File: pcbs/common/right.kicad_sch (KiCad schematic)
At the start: 89 parts, among them J2 TRS

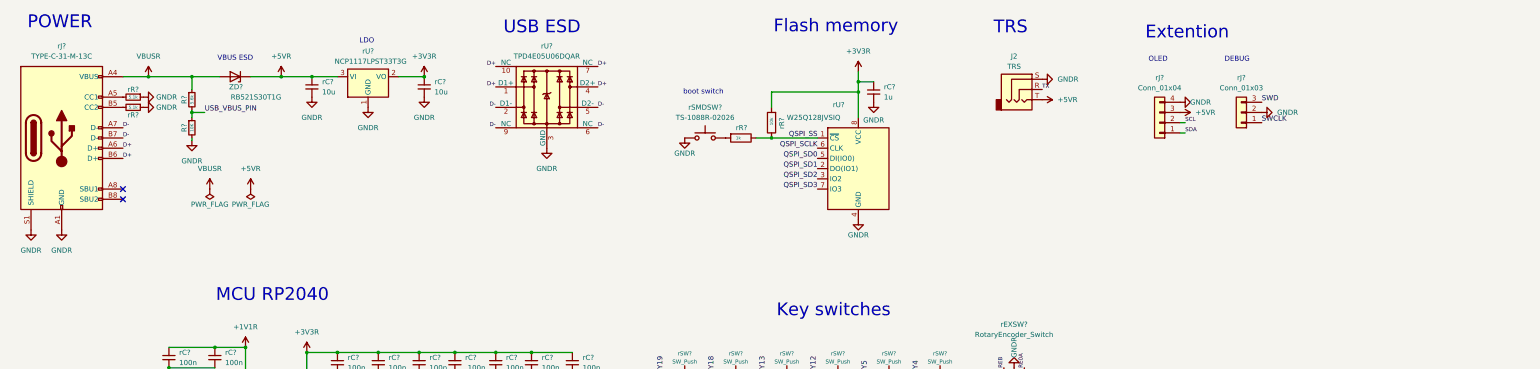
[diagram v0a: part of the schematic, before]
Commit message: Split comms through USB-C. Added more ESD.
Made a switch from TRS to USB-C for better ESD and short-circuit prevention. Added ferrite beads on external connections.
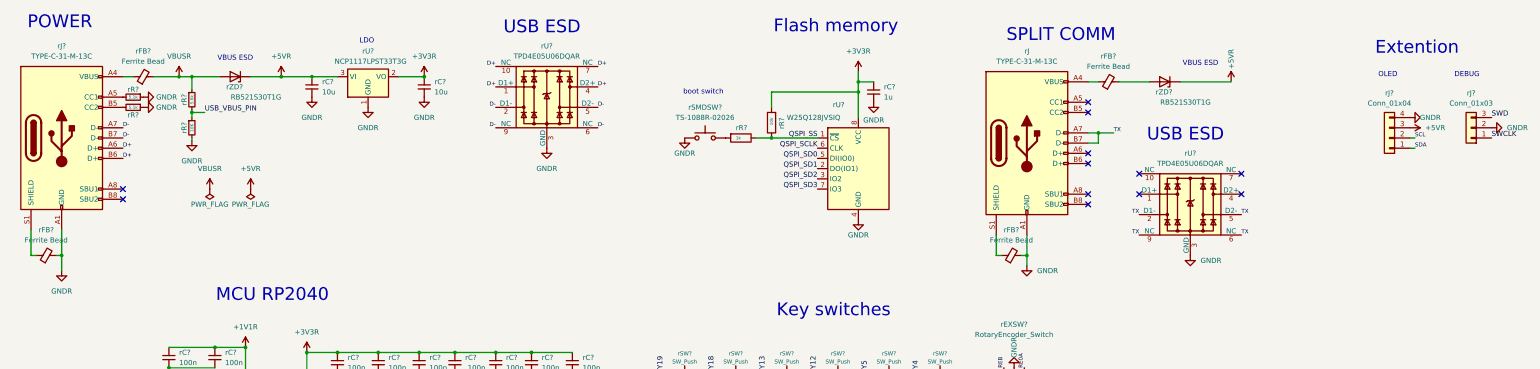
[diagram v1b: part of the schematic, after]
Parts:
- removed J2: TRS, kbd_local:PJ-398A-5A_PJ-399B-6A, symbol Connector_Audio:AudioJack3
- added rFB? (x4): Ferrite Bead, Capacitor_SMD:C_0603_1608Metric_Pad1.08x0.95mm_HandSolder, symbol Device:FerriteBead_Small
- added rJ: TYPE-C-31-M-13C, kbd_local:TYPE-C-31-M-13C, symbol kbd_local:USB_C_Receptacle_USB2.0_16P
- added rU?: TPD4E05U06DQAR, Package_SON:USON-10_2.5x1.0mm_P0.5mm, symbol Power_Protection:TPD4EUSB30
- added rZD?: RB521S30T1G, Diode_SMD:D_SOD-523, symbol Diode:ESD5Zxx
- rJ?: symbol Connector:USB_C_Receptacle_USB2.0 -> kbd_local:USB_C_Receptacle_USB2.0_16P
- gave numbers to parts that had none: 2
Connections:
- net +5VR: now also rZD?.1 (K)
- net GNDR: now also rFB?.2, rFB?.2, rJ.A1 (GND), rJ.B1 (GND), rU?.3 (GND), rU?.8 (GND); no longer rJ?.A12 (GND), rJ?.B12 (GND), rJ?.S1 (SHIELD)
- net TX: now also rJ.A7 (D-), rJ.B7 (D-), rU?.2 (D1-), rU?.5 (D2-), rU?.6 (NC), rU?.9 (NC)
- net VBUSR: now also rFB?.2; no longer rJ?.A4 (VBUS), rJ?.A9 (VBUS), rJ?.B4 (VBUS), rJ?.B9 (VBUS)
- new net: rFB?.1, rJ?.A4 (VBUS), rJ?.B4 (VBUS)
- new net: rFB?.1, rJ?.S1 (SHIELD)
- new net: rFB?.1, rJ.A4 (VBUS), rJ.B4 (VBUS)
- new net: rFB?.2, rZD?.2 (A)
- new net: rFB?.1, rJ.S1 (SHIELD)
- no-connect marks 3 -> 13
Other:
- note added: "SPLIT COMM"
- note removed: "TRS"
- moved on the sheet: rJ?

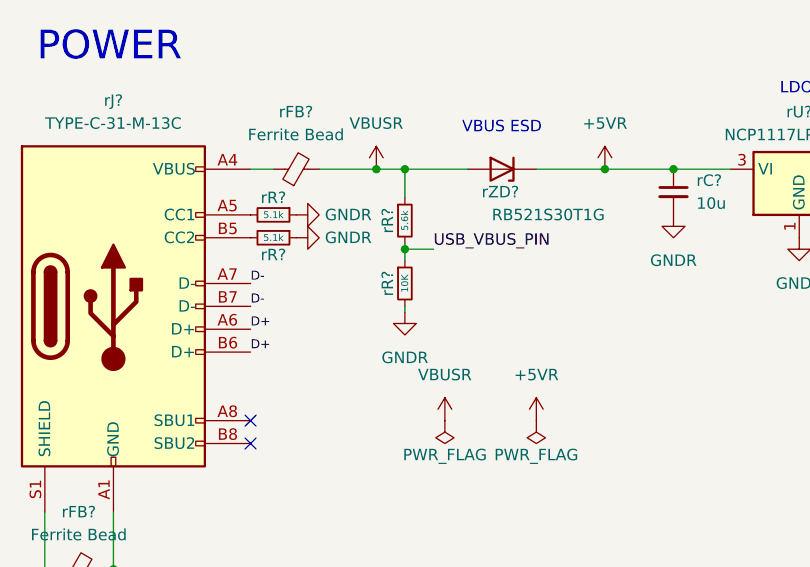
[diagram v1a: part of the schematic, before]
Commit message: fixes and preparing for pcba
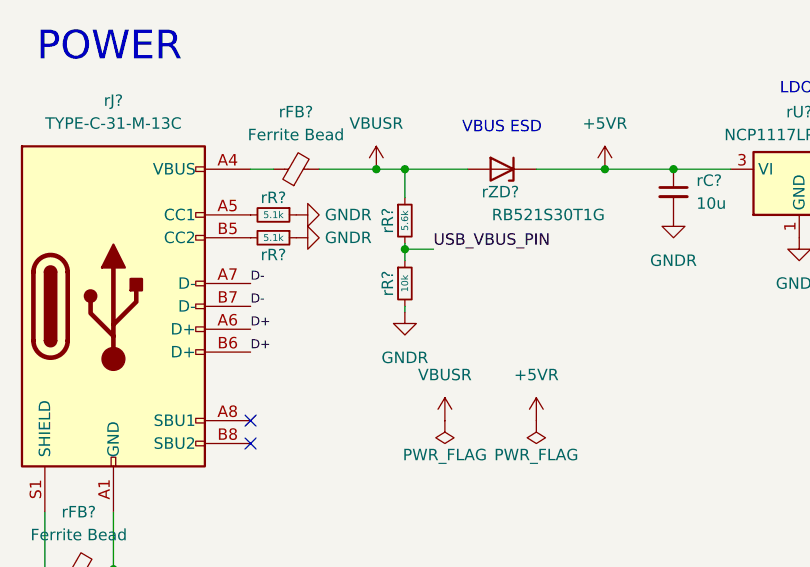
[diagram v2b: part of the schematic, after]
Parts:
- rC? (x2): LSCS Part # (none) -> C1557
- rC? (x9): LSCS Part # (none) -> C1525
- rC? (x3): LSCS Part # (none) -> C52923
- rC? (x2): LSCS Part # (none) -> C15525
- rD?: JLCPCB Part # C232841 -> (none); LSCS Part # (none) -> C232841
- rEXLED? (x2), rLED? (x21): LSCS Part # (none) -> C5149201
- rFB? (x4): JLCPCB Part # C882974 -> (none); LSCS Part # (none) -> C882974
- rJ, rJ?: JLCPCB Part # C2848620 -> (none); LSCS Part # (none) -> C2848620
- rR? (x2): LSCS Part # (none) -> C25905
- rR?: LSCS Part # (none) -> C25908
- rR? (x2): LSCS Part # (none) -> C11702
- rR?: LSCS Part # (none) -> C25744
- rR? (x2): LSCS Part # (none) -> C25100
- rR?: value 10K -> 10k; LSCS Part # (none) -> C25744
- rSMDSW? (x2): JLCPCB Part # C455280 -> (none); LSCS Part # (none) -> C455280
- rU?: JLCPCB Part # C146799 -> (none); LSCS Part # (none) -> C146799
- rU? (x2): JLCPCB Part # C138714 -> (none); LSCS Part # (none) -> C138714
- rU?: JLCPCB Part # C113767 -> (none); LSCS Part # (none) -> C113767
- rU?: JLCPCB Part # C2040 -> (none); LSCS Part # (none) -> C2040
- rY?: JLCPCB Part # C91749 -> (none); LSCS Part # (none) -> C91749
- rZD? (x2): JLCPCB Part # C145179 -> (none); LSCS Part # (none) -> C145179
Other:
- company: foostan -> tomislavrekic

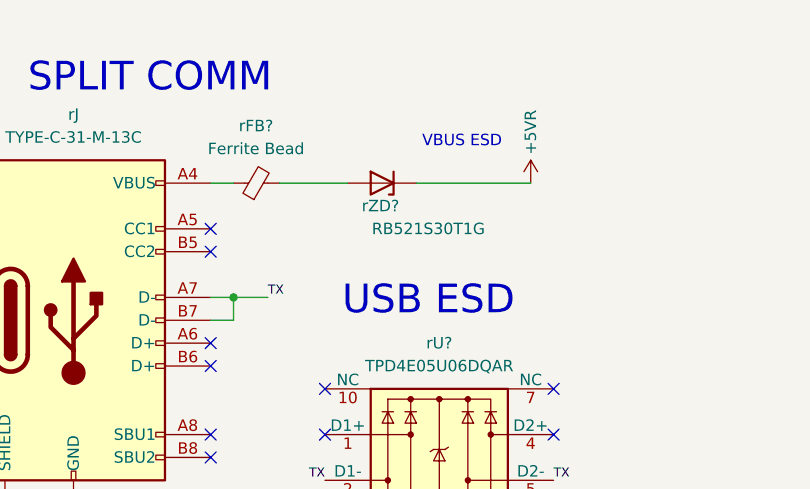
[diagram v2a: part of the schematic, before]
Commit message: Removed diode on split USB
The diode blocked power to the other half of the keyboard.
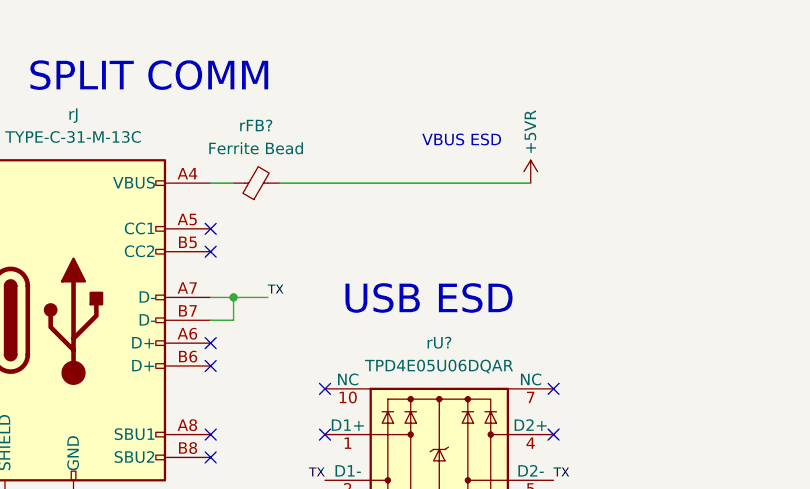
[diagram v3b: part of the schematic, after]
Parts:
- removed rZD?: RB521S30T1G, Diode_SMD:D_SOD-523, symbol Diode:ESD5Zxx
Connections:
- net +5VR: now also rFB?.2
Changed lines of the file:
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@@
 	(wire
 		(pts
-			(xy 308.61 34.29) (xy 321.31 34.29)
-		)
-		(stroke
-			(width 0)
-			(type default)
-		)
-	)
-	(wire
-		(pts
 			(xy 27.94 187.96) (xy 40.64 187.96)
 		)
@@
 	(wire
 		(pts
-			(xy 293.37 34.29) (xy 300.99 34.29)
+			(xy 293.37 34.29) (xy 321.31 34.29)
 		)
 		(stroke
@@
 					(unit 1)
 				)
-			)
-		)
-	)
-	(symbol
-		(lib_id "Diode:ESD5Zxx")
-		(at 304.8 34.29 180)
-		(unit 1)
-		(exclude_from_sim no)
-		(in_bom yes)
-		(on_board yes)
-		(dnp no)
-		(property "Reference" "rZD?"
-			(at 306.705 36.83 0)
-			(effects
-				(font
-					(size 1.27 1.27)
-				)
-				(justify left)
-			)
-		)
-		(property "Value" "RB521S30T1G"
-			(at 316.23 39.37 0)
-			(effects
-				(font
-					(size 1.27 1.27)
-				)
-				(justify left)
-			)
-		)
-		(property "Footprint" "Diode_SMD:D_SOD-523"
-			(at 304.8 29.845 0)
-			(effects
-				(font
-					(size 1.27 1.27)
-				)
-				(hide yes)
-			)
-		)
-		(property "Datasheet" ""
-			(at 304.8 34.29 0)
-			(effects
-				(font
-					(size 1.27 1.27)
-				)
-				(hide yes)
-			)
-		)
-		(property "Description" ""
-			(at 304.8 34.29 0)
-			(effects
-				(font
-					(size 1.27 1.27)
-				)
-				(hide yes)
-			)
-		)
-		(property "LSCS Part #" "C145179"
-			(at 304.8 34.29 0)
-			(effects
-				(font
-					(size 1.27 1.27)
-				)
-				(hide yes)
-			)
-		)
-		(pin "1"
-		)
-		(pin "2"
-		)
-		(instances
-			(project "right"
-				(path "/04ecfb8d-8dc8-41d9-b176-68a9b73f1e5e"
-					(reference "rZD?")
-					(unit 1)
-				)
-			)
-			(project "corne-cherry"
-				(path "/4cc5d416-57f5-4147-8183-e03ae6b1198a/50d96a5e-3d25-4129-9495-15388c76587f"
-					(reference "rZD2")
-					(unit 1)
-				)
